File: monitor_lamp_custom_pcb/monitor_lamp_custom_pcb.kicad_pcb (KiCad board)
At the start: 2 copper layers, 50 x 35 mm, 33 parts, among them IC1 HUSB238, J1 USB_C_Receptacle_PowerOnly_6P, J2 VEML7700_Connection, J3 LD2410C_Connection, J4 Conn_01x02, Q1 AO3401A, Q3 AO3400A, U1 TPS563300, U2 TPS561208DDCT, U3 ESP32-C3_SUPERMINI_TH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

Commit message: Added GND via around pcb area
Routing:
- net GND: track 13.3 -> 22.7 mm, vias 25 -> 42
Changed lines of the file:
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@@
+	)
+	(segment
+		(start 124.1 56)
+		(end 125 56)
+		(width 0.2)
+		(layer "F.Cu")
+		(net "GND")
+	)
+	(segment
+		(start 125 56)
+		(end 125.65 56.65)
+		(width 0.2)
+		(layer "F.Cu")
+		(net "GND")
+	)
+	(segment
+		(start 126.235 57.235)
+		(end 126.235 58.62)
+		(width 0.2)
+		(layer "F.Cu")
+		(net "GND")
 	)
 	(segment
@@
 	)
 	(segment
+		(start 120.735 57.165)
+		(end 121.3 56.6)
+		(width 0.2)
+		(layer "F.Cu")
+		(net "GND")
+	)
+	(segment
 		(start 117.325 60.075)
 		(end 117.4 60)
@@
 	)
 	(segment
+		(start 121.9 56)
+		(end 122.7 56)
+		(width 0.2)
+		(layer "F.Cu")
+		(net "GND")
+	)
+	(segment
 		(start 147.85 56.55)
 		(end 147.8 56.6)
@@
 	)
 	(segment
+		(start 125.65 56.65)
+		(end 126.235 57.235)
+		(width 0.2)
+		(layer "F.Cu")
+		(net "GND")
+	)
+	(segment
+		(start 120.735 58.62)
+		(end 120.735 57.165)
+		(width 0.2)
+		(layer "F.Cu")
+		(net "GND")
+	)
+	(segment
+		(start 122.7 56)
+		(end 124.1 56)
+		(width 0.2)
+		(layer "F.Cu")
+		(net "GND")
+	)
+	(segment
 		(start 118 69.8)
 		(end 118 70.245)
@@
 		(net "GND")
 	)
+	(segment
+		(start 121.3 56.6)
+		(end 121.9 56)
+		(width 0.2)
+		(layer "F.Cu")
+		(net "GND")
+	)
+	(via
+		(at 146 54.7)
+		(size 0.6)
+		(drill 0.3)
+		(layers "F.Cu" "B.Cu")
+		(free yes)
+		(net "GND")
+	)
 	(via
 		(at 137.7 86.2)
@@
 	)
 	(via
+		(at 121.3 56.6)
+		(size 0.6)
+		(drill 0.3)
+		(layers "F.Cu" "B.Cu")
+		(net "GND")
+	)
+	(via
 		(at 144.1 77.8)
 		(size 0.6)
@@
 	)
 	(via
+		(at 117.7 86.2)
+		(size 0.6)
+		(drill 0.3)
+		(layers "F.Cu" "B.Cu")
+		(free yes)
+		(net "GND")
+	)
+	(via
 		(at 136 72.3)
 		(size 0.6)
@@
 	)
 	(via
+		(at 117.3 56.4)
+		(size 0.6)
+		(drill 0.3)
+		(layers "F.Cu" "B.Cu")
+		(free yes)
+		(net "GND")
+	)
+	(via
 		(at 148.2 77.8)
 		(size 0.6)
@@
 	)
 	(via
+		(at 164.4 72.9)
+		(size 0.6)
+		(drill 0.3)
+		(layers "F.Cu" "B.Cu")
+		(free yes)
+		(net "GND")
+	)
+	(via
 		(at 134.9 77.2)
 		(size 0.6)
@@
 	)
 	(via
+		(at 122.7 56)
+		(size 0.6)
+		(drill 0.3)
+		(layers "F.Cu" "B.Cu")
+		(net "GND")
+	)
+	(via
 		(at 132.1 65.9)
 		(size 0.6)
@@
 	)
 	(via
+		(at 144.7 86.8)
+		(size 0.6)
+		(drill 0.3)
+		(layers "F.Cu" "B.Cu")
+		(free yes)
+		(net "GND")
+	)
+	(via
 		(at 131 56.9)
 		(size 0.6)
@@
 	)
 	(via
+		(at 160.5 54.6)
+		(size 0.6)
+		(drill 0.3)
+		(layers "F.Cu" "B.Cu")
+		(free yes)
+		(net "GND")
+	)
+	(via
 		(at 117.4 60)
 		(size 0.6)
@@
 	)
 	(via
+		(at 125.65 56.65)
+		(size 0.6)
+		(drill 0.3)
+		(layers "F.Cu" "B.Cu")
+		(net "GND")
+	)
+	(via
 		(at 130.8 65.9)
 		(size 0.6)
@@
 	)
 	(via
+		(at 117.3 79.9)
+		(size 0.6)
+		(drill 0.3)
+		(layers "F.Cu" "B.Cu")
+		(free yes)
+		(net "GND")
+	)
+	(via
+		(at 164.3 81)
+		(size 0.6)
+		(drill 0.3)
+		(layers "F.Cu" "B.Cu")
+		(free yes)
+		(net "GND")
+	)
+	(via
 		(at 145.5 77.8)
 		(size 0.6)
@@
 	)
 	(via
+		(at 132.6 54.7)
+		(size 0.6)
+		(drill 0.3)
+		(layers "F.Cu" "B.Cu")
+		(free yes)
+		(net "GND")
+	)
+	(via
+		(at 117.2 65.3)
+		(size 0.6)
+		(drill 0.3)
+		(layers "F.Cu" "B.Cu")
+		(free yes)
+		(net "GND")
+	)
+	(via
 		(at 117.4 69.2)
 		(size 0.6)
@@
 	)
 	(via
+		(at 124.1 56)
+		(size 0.6)
+		(drill 0.3)
+		(layers "F.Cu" "B.Cu")
+		(net "GND")
+	)
+	(via
+		(at 137.6 54.7)
+		(size 0.6)
+		(drill 0.3)
+		(layers "F.Cu" "B.Cu")
+		(free yes)
+		(net "GND")
+	)
+	(via
 		(at 126.3 73.1)
 		(size 0.6)
@@
 	)
 	(via
+		(at 124.9 86.4)
+		(size 0.6)
+		(drill 0.3)
+		(layers "F.Cu" "B.Cu")
+		(free yes)
+		(net "GND")
+	)
+	(via
 		(at 147.8 56.55)
 		(size 0.6)
@@
 		(net "GND")
 	)
+	(via
+		(at 154.7 54.7)
+		(size 0.6)
+		(drill 0.3)
+		(layers "F.Cu" "B.Cu")
+		(free yes)
+		(net "GND")
+	)

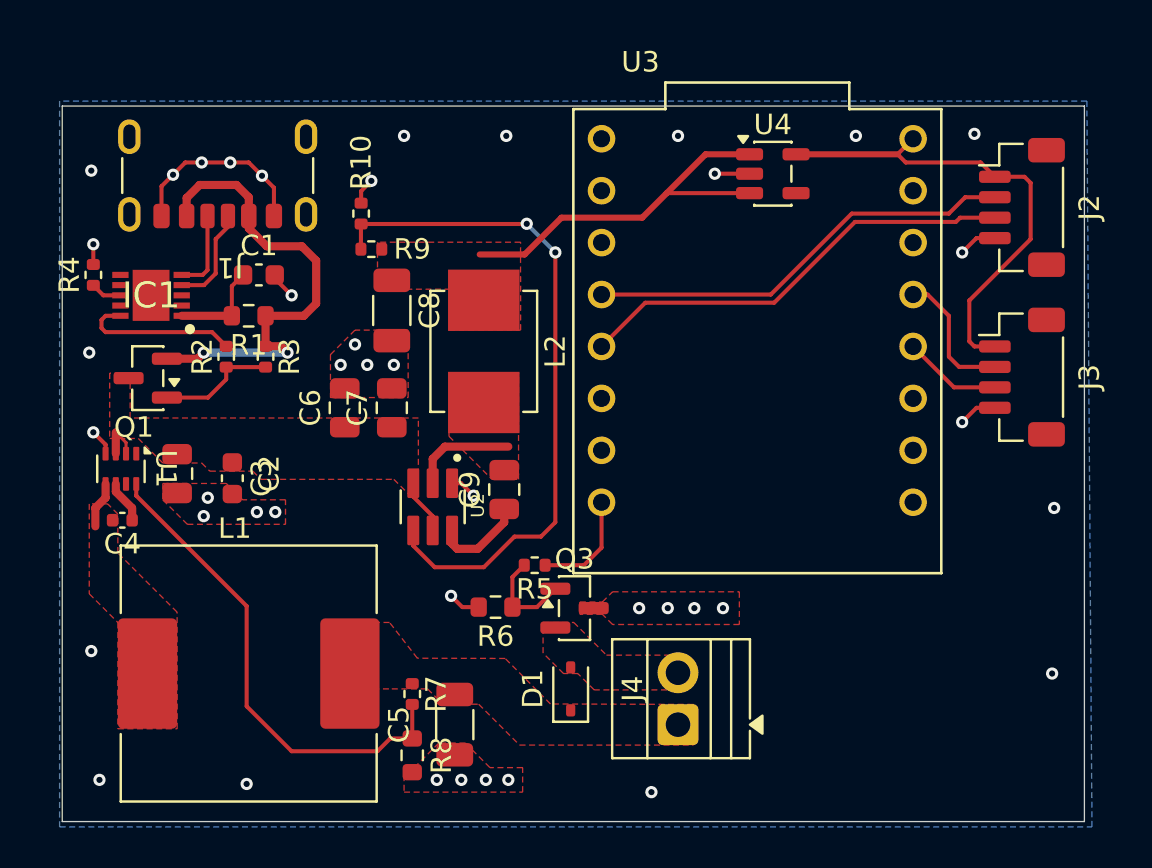
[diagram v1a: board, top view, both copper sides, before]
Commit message: Added connection for temp sensor
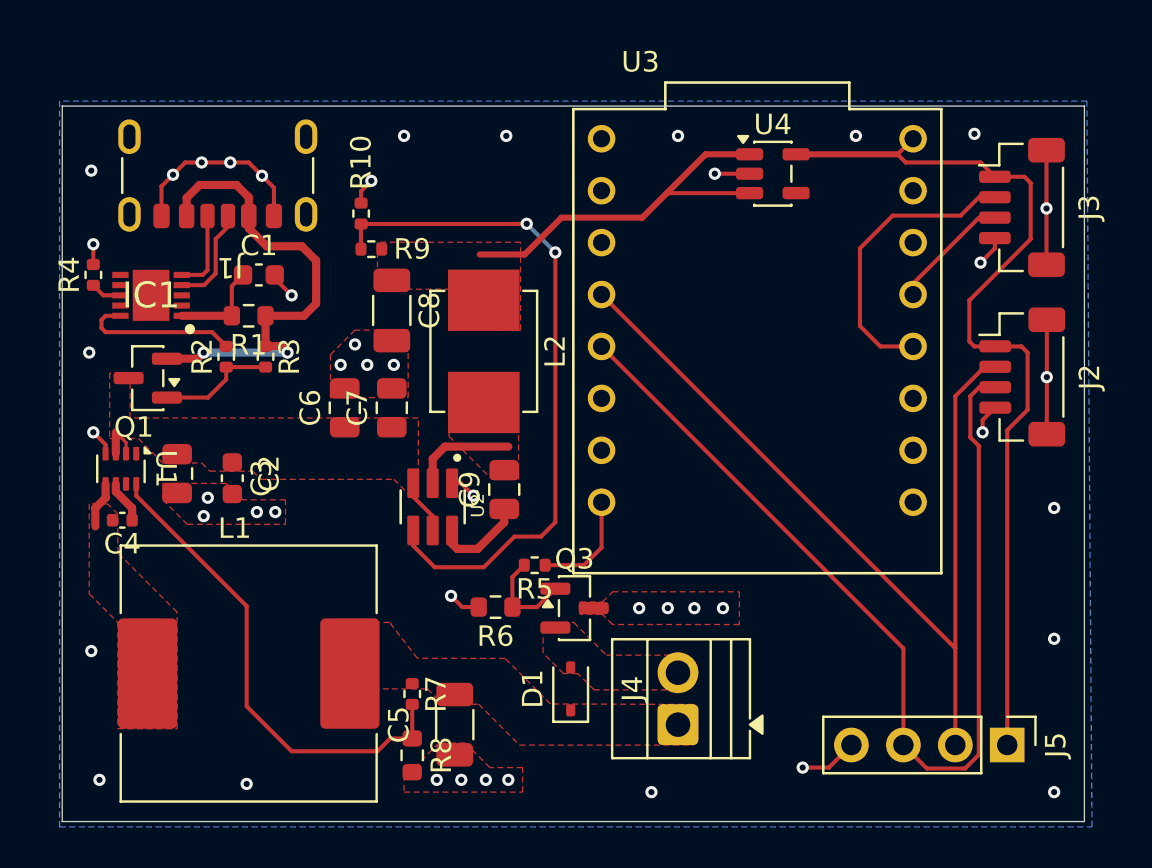
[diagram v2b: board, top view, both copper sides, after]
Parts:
- added J5: SHTxx_Connection, Connector_PinHeader_2.54mm:PinHeader_1x04_P2.54mm_Vertical, F.Cu at (162.1, 84.5)
- moved J3 8.30 mm to (162.8, 58.2)
- moved J2 8.29 mm to (162.8, 66.5)
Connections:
- J2 pad MP: (no net) -> GND
- J3 pad MP: (no net) -> GND
- U3 pad 3: Net-(J3-Pin_3) -> Net-(J3-Pin_2)
- U3 pad 4: Net-(J3-Pin_2) -> Net-(J3-Pin_3)
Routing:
- net /ESP32_Sensors_Mosfet/SCL: track 21.8 -> 49.2 mm
- net /ESP32_Sensors_Mosfet/SDA: track 21.2 -> 44.1 mm
- net /ESP32_Sensors_Mosfet/5V_Protected: track 23.5 -> 44.8 mm
- net GND: track 22.7 -> 35.9 mm, vias 42 -> 46
- net Net-(J3-Pin_2): track 6.64 -> 14.4 mm
- net Net-(J3-Pin_3): track 4.83 -> 5.87 mm

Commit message: Added supplementary power supply connection
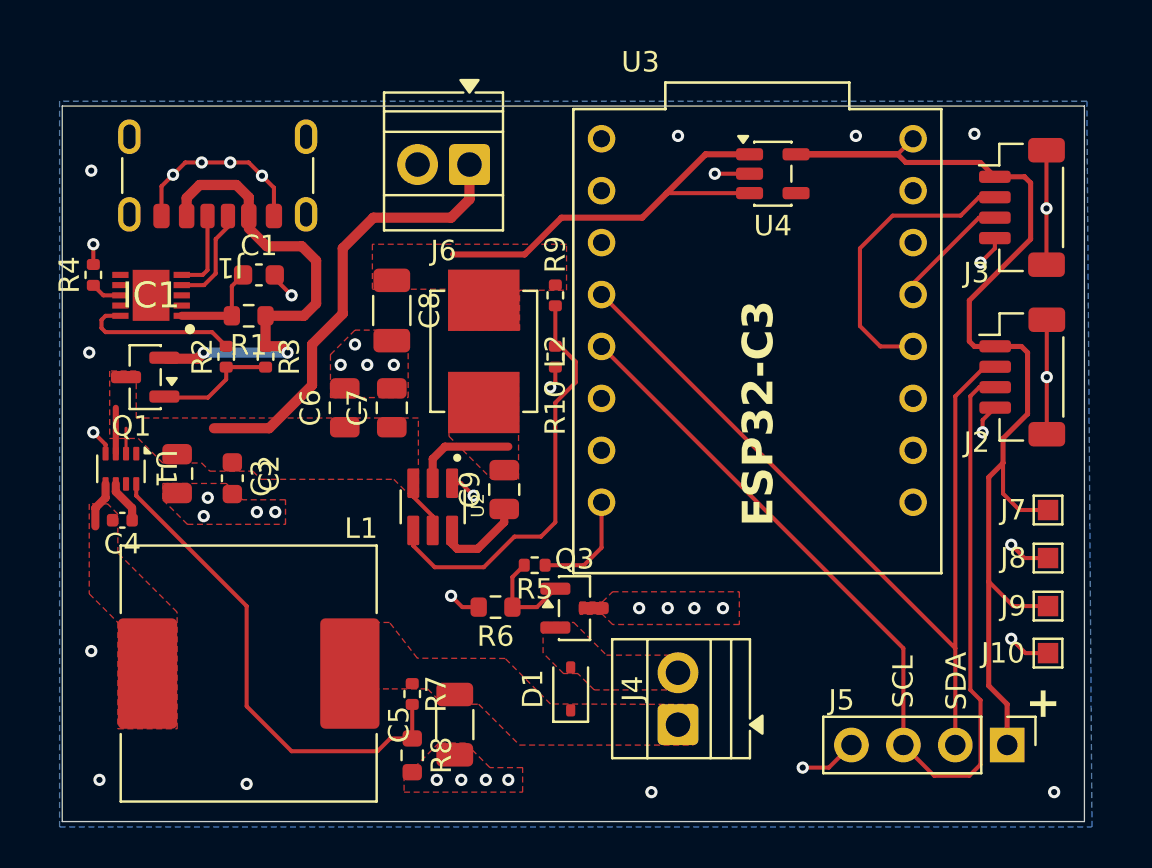
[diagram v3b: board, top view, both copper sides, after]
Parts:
- added J10: Conn_01x01, TestPoint:TestPoint_Pad_1.0x1.0mm, F.Cu at (164.1, 80.0)
- added J6: Direct_power_supply, TerminalBlock:TerminalBlock_Xinya_XY308-2.54-2P_1x02_P2.54mm_Horizontal, F.Cu at (135.8, 56.1)
- added J7: Conn_01x01, TestPoint:TestPoint_Pad_1.0x1.0mm, F.Cu at (164.1, 73.0)
- added J8: Conn_01x01, TestPoint:TestPoint_Pad_1.0x1.0mm, F.Cu at (164.1, 75.3)
- added J9: Conn_01x01, TestPoint:TestPoint_Pad_1.0x1.0mm, F.Cu at (164.1, 77.7)
- moved R10 11.8 mm to (140.0, 65.5), turned to -90 degrees
- moved R9 9.28 mm to (140.0, 62.5), turned to -90 degrees
- moved Q1 0.13 mm to (119.9, 66.5)
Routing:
- net /+15V: track 5.00 -> 28.1 mm
- net Net-(U2-VFB): track 33.6 -> 20.6 mm, vias 2 -> 0
- net /ESP32_Sensors_Mosfet/5V_Protected: track 44.8 -> 53.0 mm
- net GND: track 35.9 -> 40.4 mm, vias 46 -> 44
- net /+5V: track 19.3 -> 20.6 mm
- net /ESP32_Sensors_Mosfet/SCL: track 49.2 -> 49.9 mm
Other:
- board text added: "+"
- board text added: "ESP32-C3"
- board text added: "SCL"
- board text added: "SDA"

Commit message: Some test
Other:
- board text added: "ESP32-C3 Supermini"
- board text removed: "ESP32-C3"
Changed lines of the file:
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@@
 		)
 	)
-	(gr_text "ESP32-C3"
-		(at 150.8 73.8 90)
+	(gr_text "ESP32-C3\nSupermini"
+		(at 152 72.8 90)
 		(layer "F.SilkS")
 		(effects

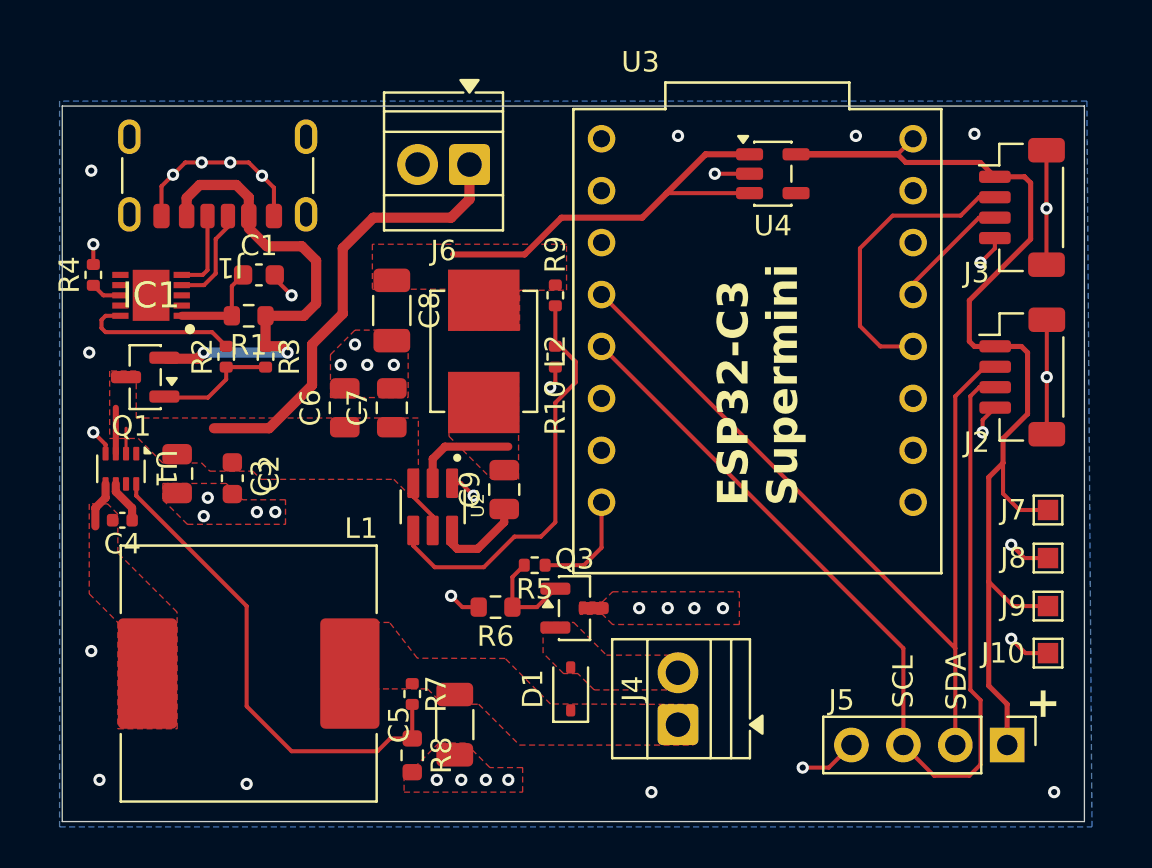
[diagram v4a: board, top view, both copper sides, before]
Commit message: Corrected position and writing of graphical layer
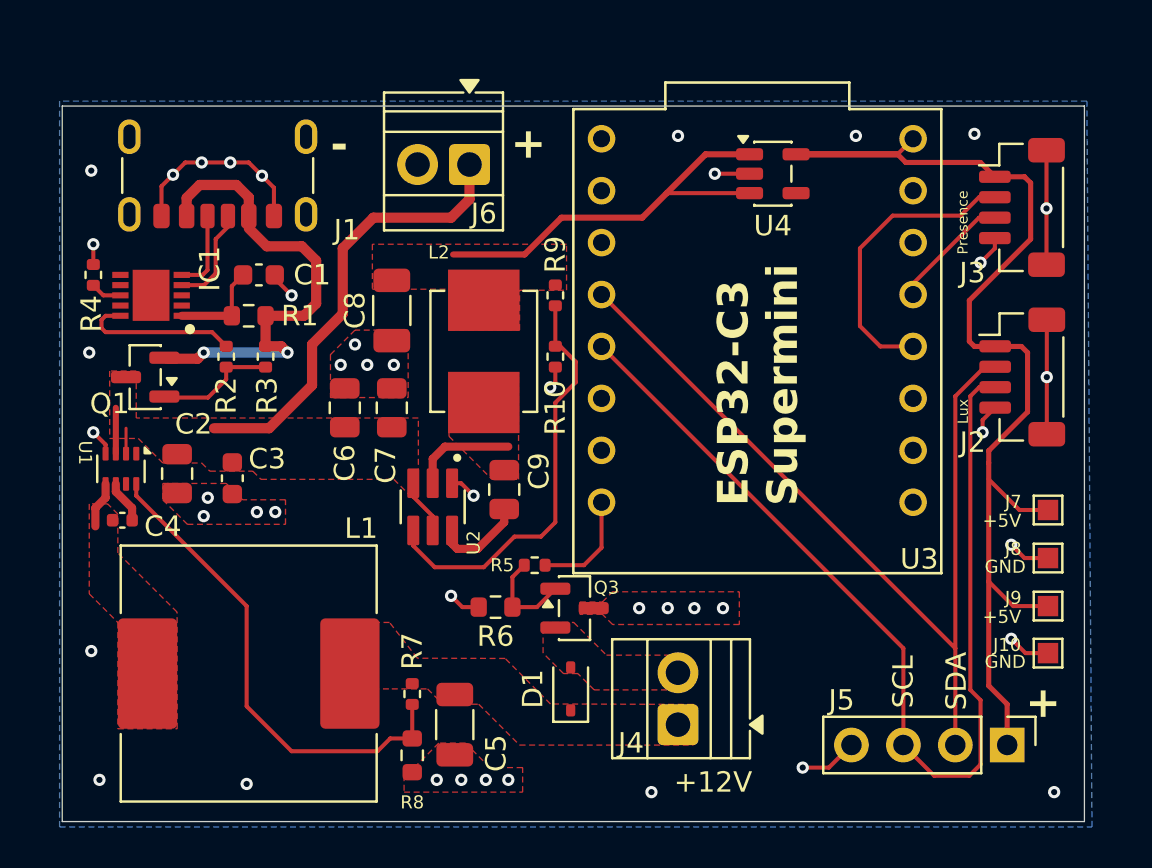
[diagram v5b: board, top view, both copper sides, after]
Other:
- board text added: "+12V"
- board text added: "+5V"
- board text added: "-"
- board text added: "GND"
- board text added: "Lux"
- board text added: "Presence"

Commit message: Changed all resistors footprint to R_0603_1608 metric
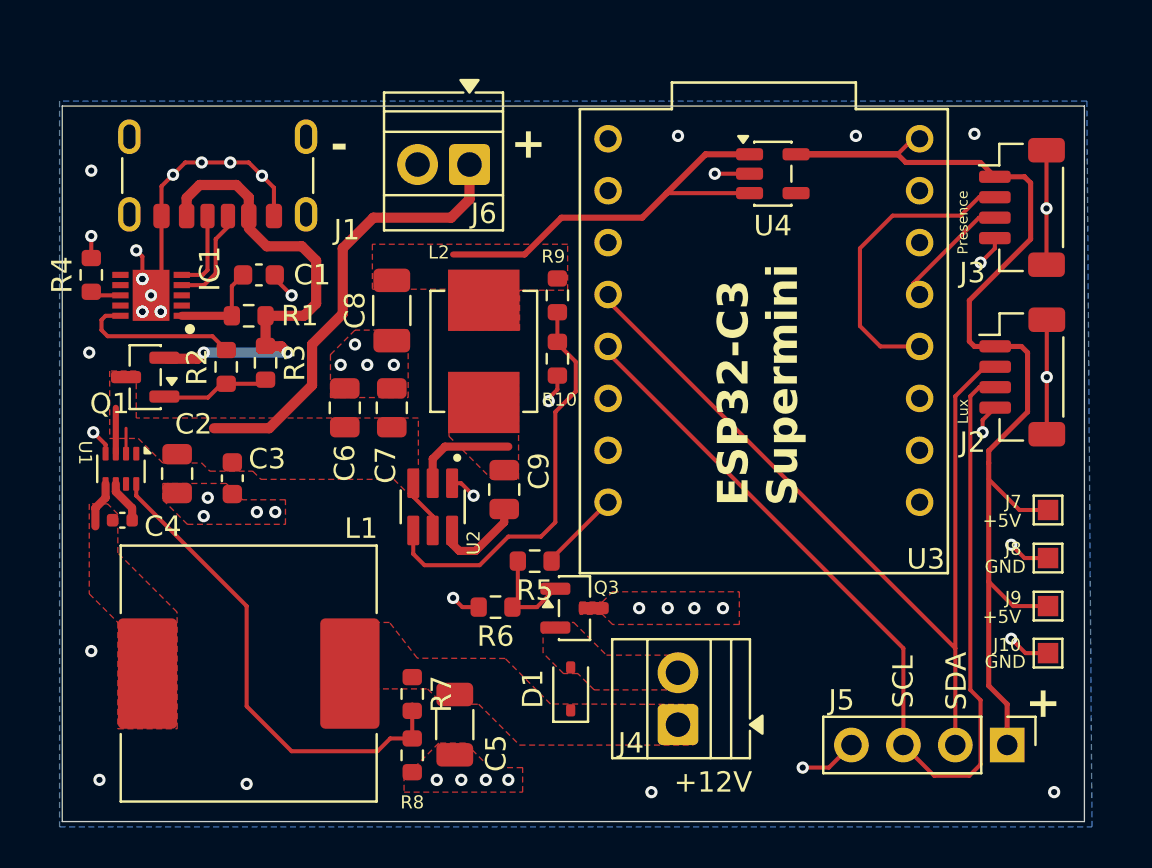
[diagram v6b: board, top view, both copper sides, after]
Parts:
- R10, R2, R3, R4, R5, R7, R9: footprint Resistor_SMD:R_0402_1005Metric -> Resistor_SMD:R_0603_1608Metric
- moved R2 0.50 mm to (123.9, 66.0)
- moved U3 0.32 mm to (150.2, 64.7)
- moved R3 0.30 mm to (125.8, 65.8)
- moved R5 0.20 mm to (139.0, 75.5)
- moved R10 0.14 mm to (140.1, 65.6)
- moved R4 0.10 mm to (117.3, 61.5)
- moved R9 0.10 mm to (140.1, 62.5)
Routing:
- net GND: track 40.4 -> 46.6 mm, vias 44 -> 52
- net PWM_Control: track 5.34 -> 4.03 mm
- net Net-(Q1-G): track 5.79 -> 5.19 mm

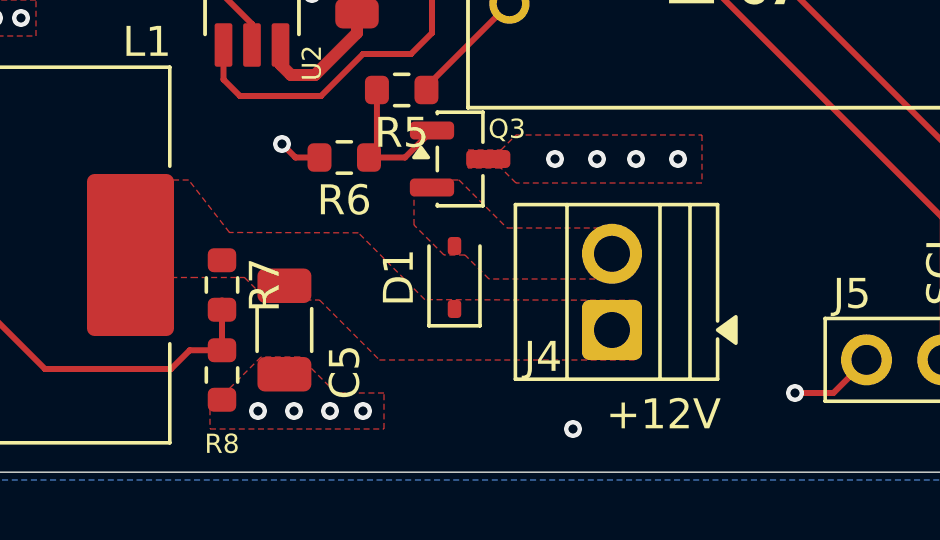
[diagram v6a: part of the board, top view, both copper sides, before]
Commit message: Added some LCSC to the components
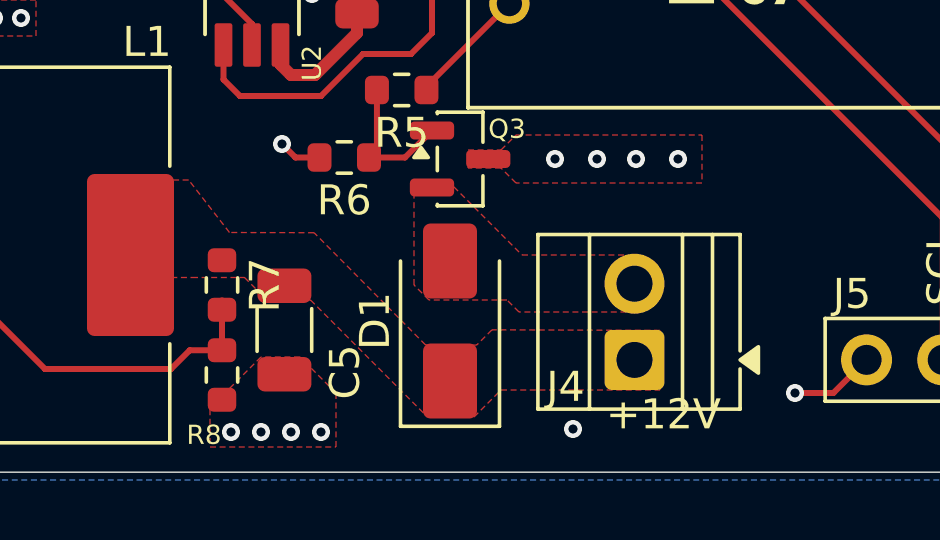
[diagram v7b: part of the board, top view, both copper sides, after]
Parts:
- D1: value 1N5819WS -> SS34; footprint Diode_SMD:D_SOD-323 -> Diode_SMD:D_SMA
- moved D1 1.46 mm to (140.6, 83.2)
- moved J4 1.25 mm to (146.7, 84.5)
